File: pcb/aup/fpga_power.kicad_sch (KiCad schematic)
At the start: 5 parts, among them U1 XC7A50T-FGG484, U15 TPS2116DRLR

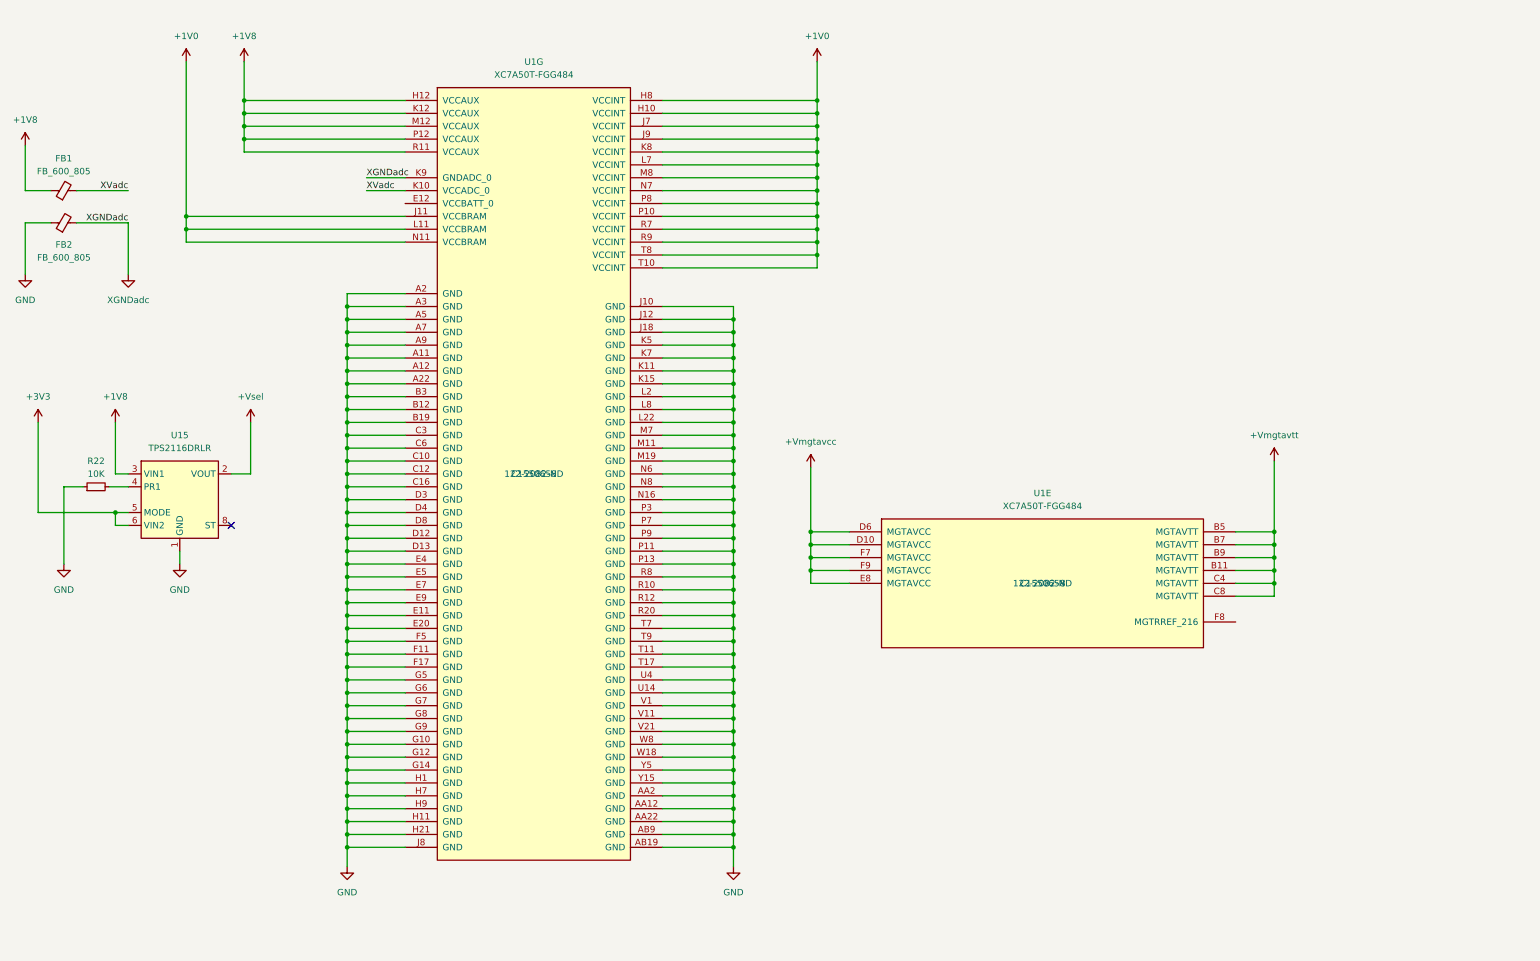
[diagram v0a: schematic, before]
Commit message: Add hierarchical sheets for banks and add caps.
There are some stale sheets in this commit, but I don't want to delete
an active one accidentally. Save them all for now, and then go back and
clean them up.
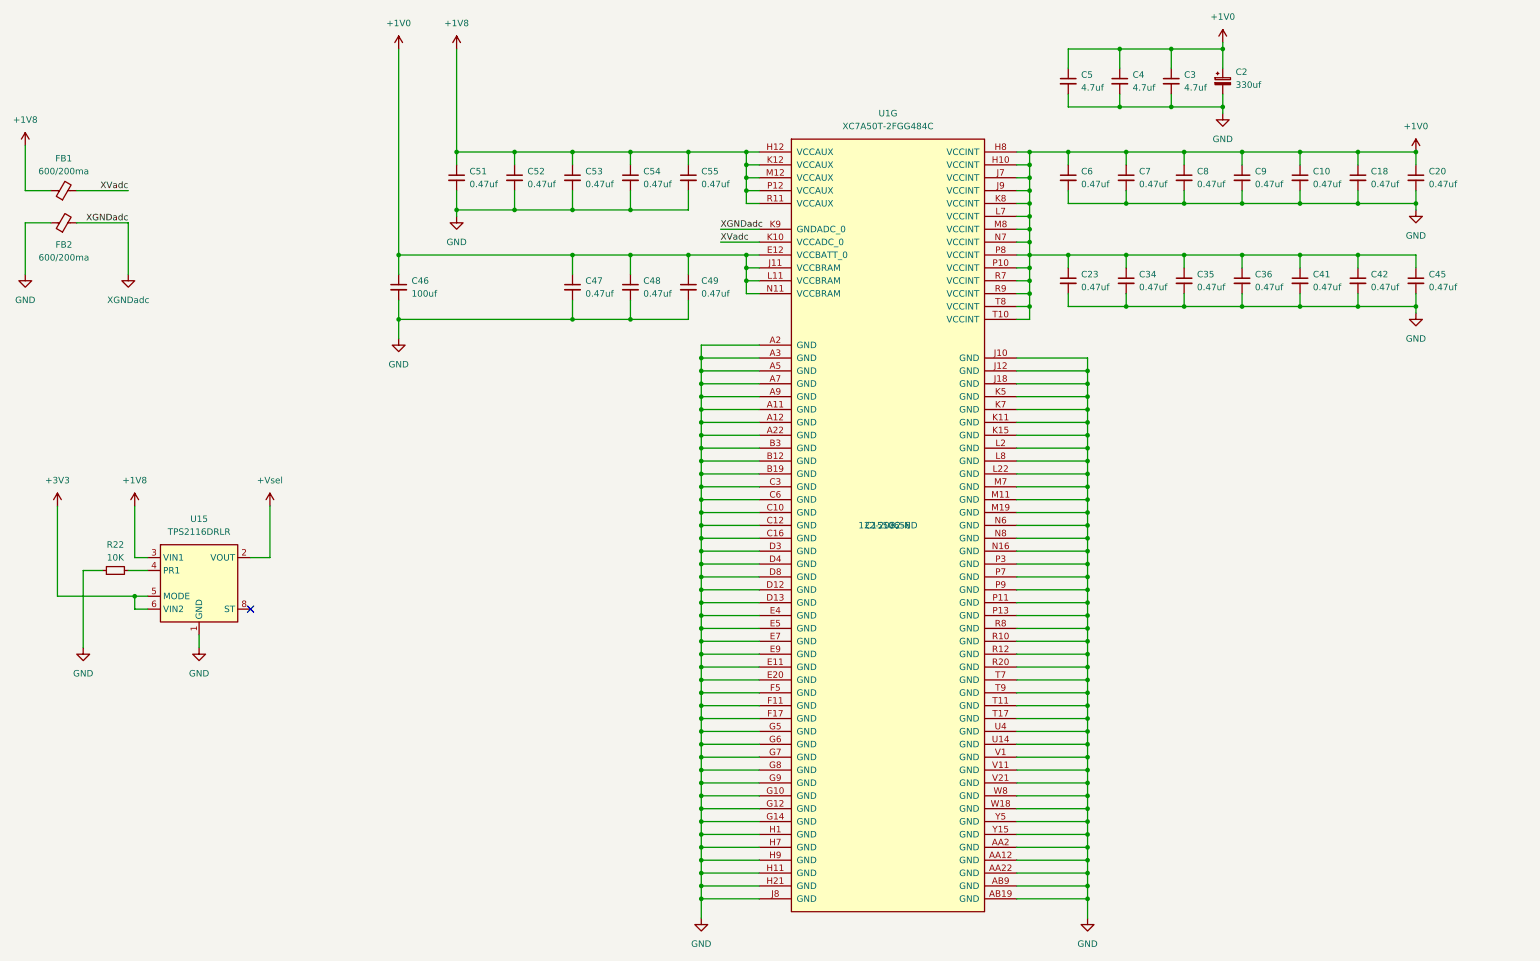
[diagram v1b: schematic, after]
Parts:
- removed unit 5 of U1
- added C10, C18, C20, C23, C34, C35, C36, C41, C42, C45, C47, C48, C49, C51, C52, C53, C54, C55, C6, C7, C8, C9: 0.47uf, Capacitor_SMD:C_0402_1005Metric, symbol !Misc:C_0.47uf_0402
- added C2: 330uf, !Misc:T520V, symbol !Misc:C_330uf_2917_T
- added C3, C4, C5: 4.7uf, Capacitor_SMD:C_0805_2012Metric, symbol !Misc:C_4.7uf_0805
- added C46: 100uf, Capacitor_SMD:C_1206_3216Metric, symbol !Misc:C_100uf_1206
- FB1, FB2: value FB_600_805 -> 600/200ma; footprint Inductor_SMD:L_0805_2012Metric -> Inductor_SMD:L_0603_1608Metric; Digi-Key Part Number 240-2399-1-ND -> 240-2371-1-ND; LCSC Part # C1017 -> C1002
- U1: value XC7A50T-FGG484 -> XC7A50T-2FGG484C
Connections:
- net +1V0: now also U1.E12 (VCCBATT_0), C10.1, C18.1, C2.1, C20.1, C23.1, C3.1, C34.1, C35.1, C36.1, C4.1, C41.1, C42.1, C45.1, C46.1, C47.1, C48.1, C49.1, C5.1, C6.1, C7.1, C8.1, C9.1
- net +1V8: now also C51.1, C52.1, C53.1, C54.1, C55.1
- net GND: now also C10.2, C18.2, C2.2, C20.2, C23.2, C3.2, C34.2, C35.2, C36.2, C4.2, C41.2, C42.2, C45.2, C46.2, C47.2, C48.2, C49.2, C5.2, C51.2, C52.2, C53.2, C54.2, C55.2, C6.2, C7.2, C8.2, C9.2
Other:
- moved on the sheet: R22, U15, U1G

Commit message: Added more passives
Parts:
- added C100, C99: 4.7uf, Capacitor_SMD:C_0805_2012Metric, symbol !Misc:C_4.7uf_0805
- added C101: 47uf, Capacitor_SMD:C_1206_3216Metric, symbol !Misc:C_47uf_1206
- added C50: 0.47uf, Capacitor_SMD:C_0402_1005Metric, symbol !Misc:C_0.47uf_0402
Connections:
- net +1V0: now also C50.1
- net +1V8: now also C100.1, C101.1, C99.1
- net GND: now also C100.2, C101.2, C50.2, C99.2
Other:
- moved on the sheet: C46

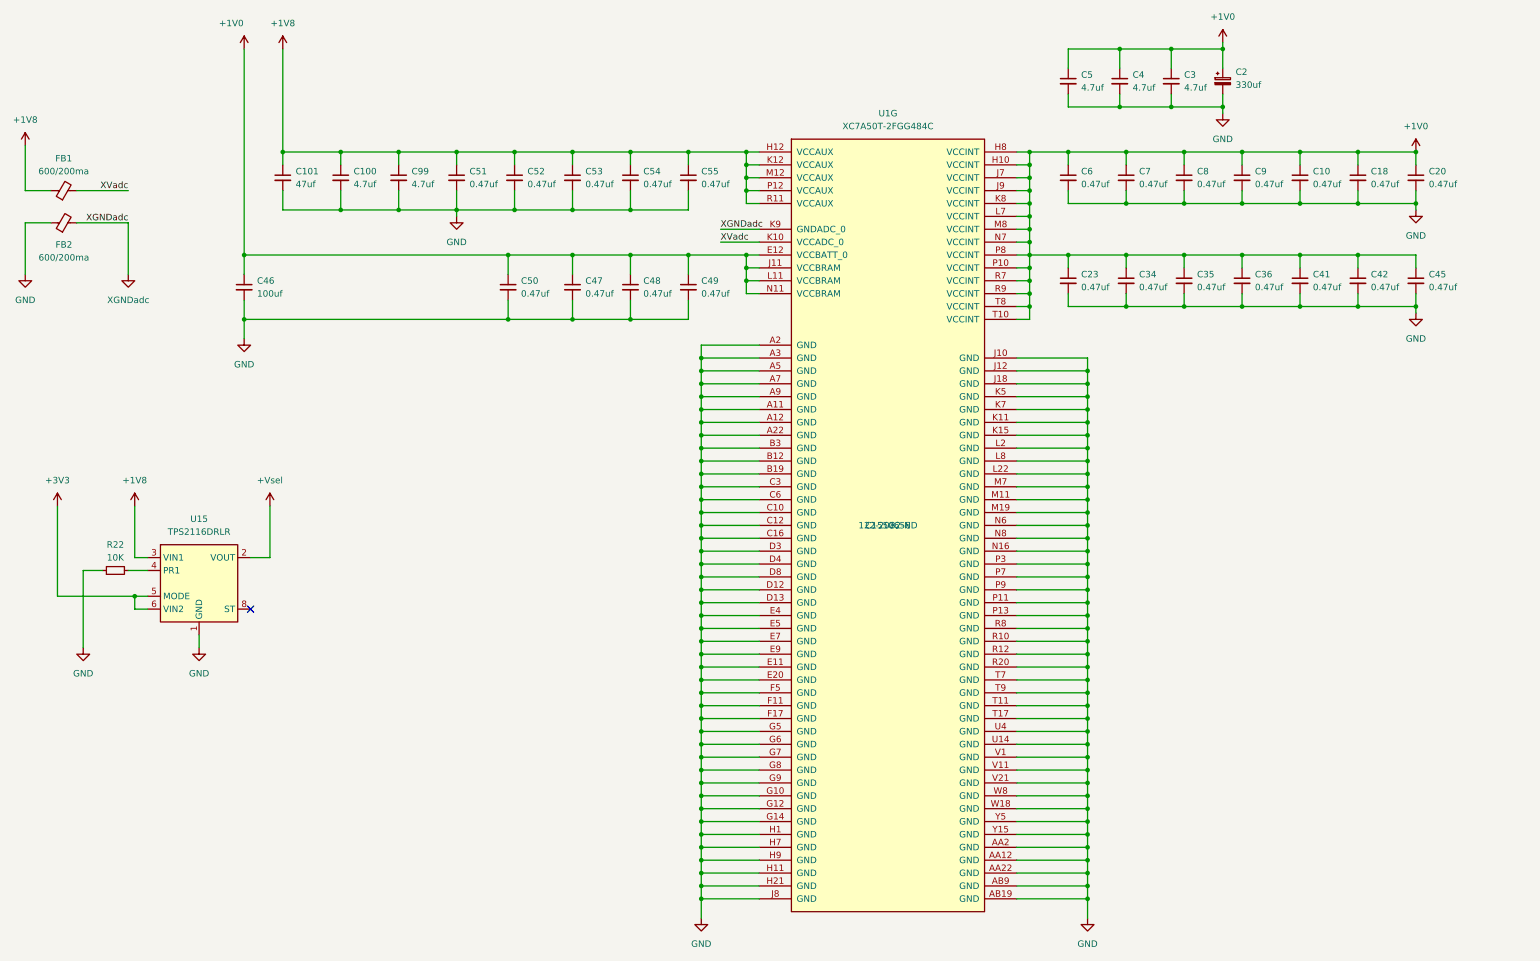
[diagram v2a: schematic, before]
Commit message: Switch 0.47uf caps under bga to 0201
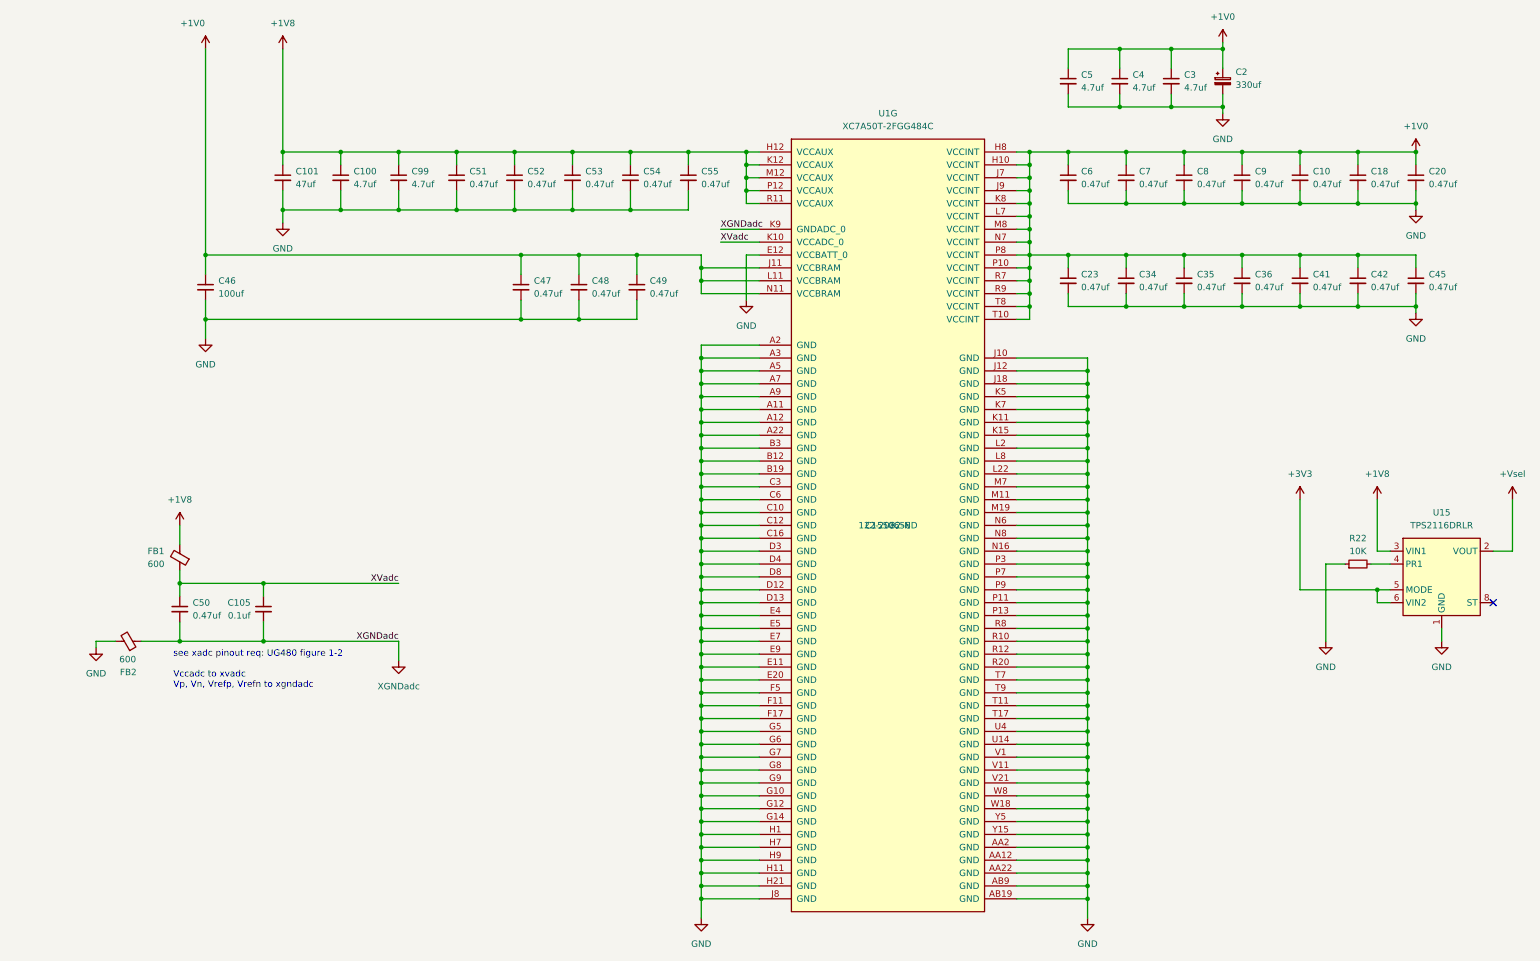
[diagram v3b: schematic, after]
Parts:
- removed C50: 0.47uf, Capacitor_SMD:C_0402_1005Metric, symbol !Misc:C_0.47uf_0402
- added C105: 0.1uf, Capacitor_SMD:C_0402_1005Metric, symbol !Misc:C_0.1uf_0402
- added C50: 0.47uf, Capacitor_SMD:C_0201_0603Metric, symbol !Misc:C_0.47uf_0201
- C10, C18, C20, C23, C34, C35, C36, C41, C42, C45, C47, C48, C49, C51, C52, C53, C54, C55, C6, C7, C8, C9: footprint Capacitor_SMD:C_0402_1005Metric -> Capacitor_SMD:C_0201_0603Metric; symbol !Misc:C_0.47uf_0402 -> !Misc:C_0.47uf_0201; Digi-Key Part Number 1276-1173-1-ND -> 1276-1337-1-ND; LCSC Part # C1779 -> C318543
- FB1, FB2: value 600/200ma -> 600; footprint Inductor_SMD:L_0603_1608Metric -> Inductor_SMD:L_0402_1005Metric; symbol !Misc:FB_600 -> !Misc:FB_600_0402; Digi-Key Part Number 240-2371-1-ND -> 490-5441-1-ND; LCSC Part # C1002 -> C76886
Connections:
- net +1V0: no longer U1.E12 (VCCBATT_0)
- net +1V8: now also FB1.2; no longer FB1.1
- net GND: now also FB2.2, U1.E12 (VCCBATT_0); no longer FB2.1
- net XGNDadc: now also FB2.1, C105.2, C50.2; no longer FB2.2
- net XVadc: now also FB1.1, C105.1, C50.1; no longer FB1.2
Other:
- note added: "see xadc pinout req: UG480 figure 1-2 Vccadc to xvadc Vp, Vn, Vrefp, Vrefn to xgndadc"
- moved on the sheet: C46, C47, C48, C49, FB1, FB2, R22, U15
